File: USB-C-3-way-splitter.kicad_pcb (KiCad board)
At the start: 2 copper layers, 31 x 33 mm, 33 parts, among them J1 USB_C_Receptacle_USB2.0, J2 Conn_01x05_Socket, J3 Conn_01x05_Socket, J4 Conn_01x05_Socket, U1 LM393, U2 SiP32509

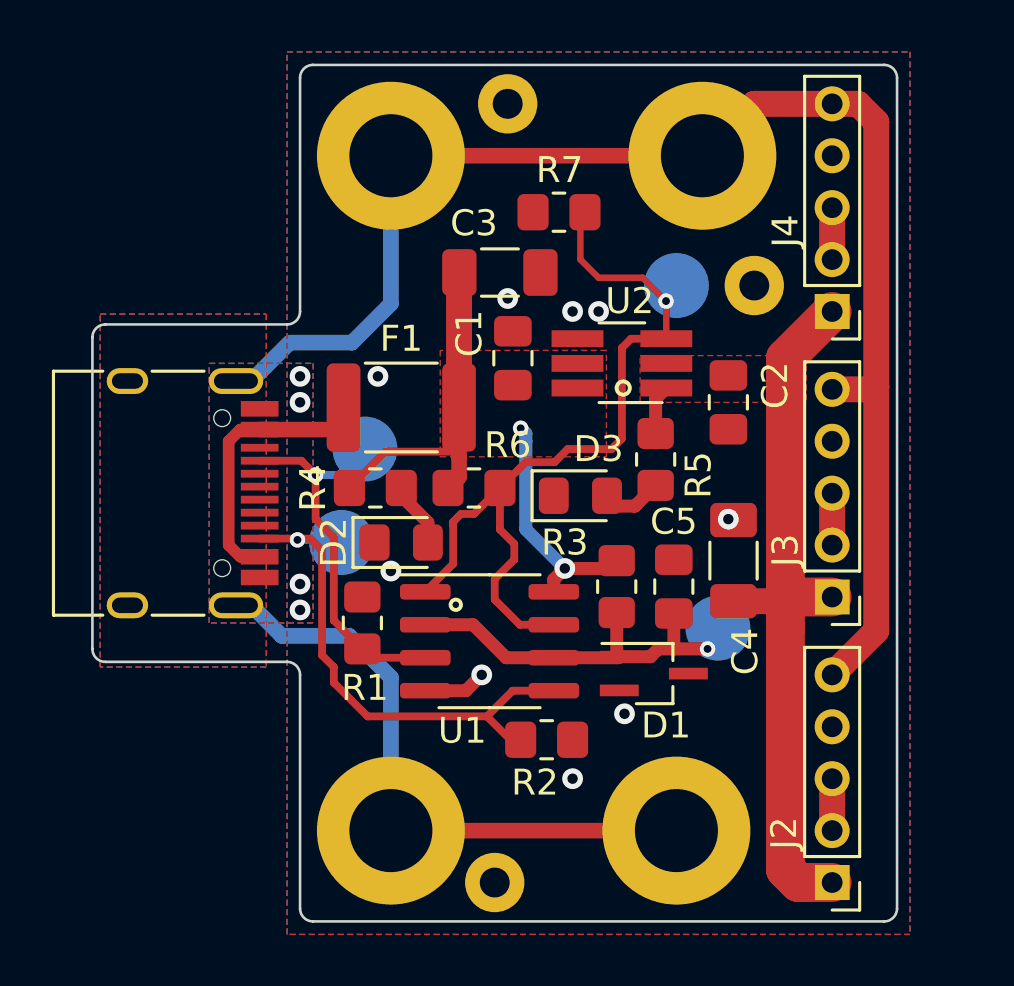
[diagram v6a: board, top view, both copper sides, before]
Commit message: Redesigned to fix circuit design error
The previous revision had the comparator outputs implemented as an AND instead of an OR, which was preventing the switch from ever turning on.
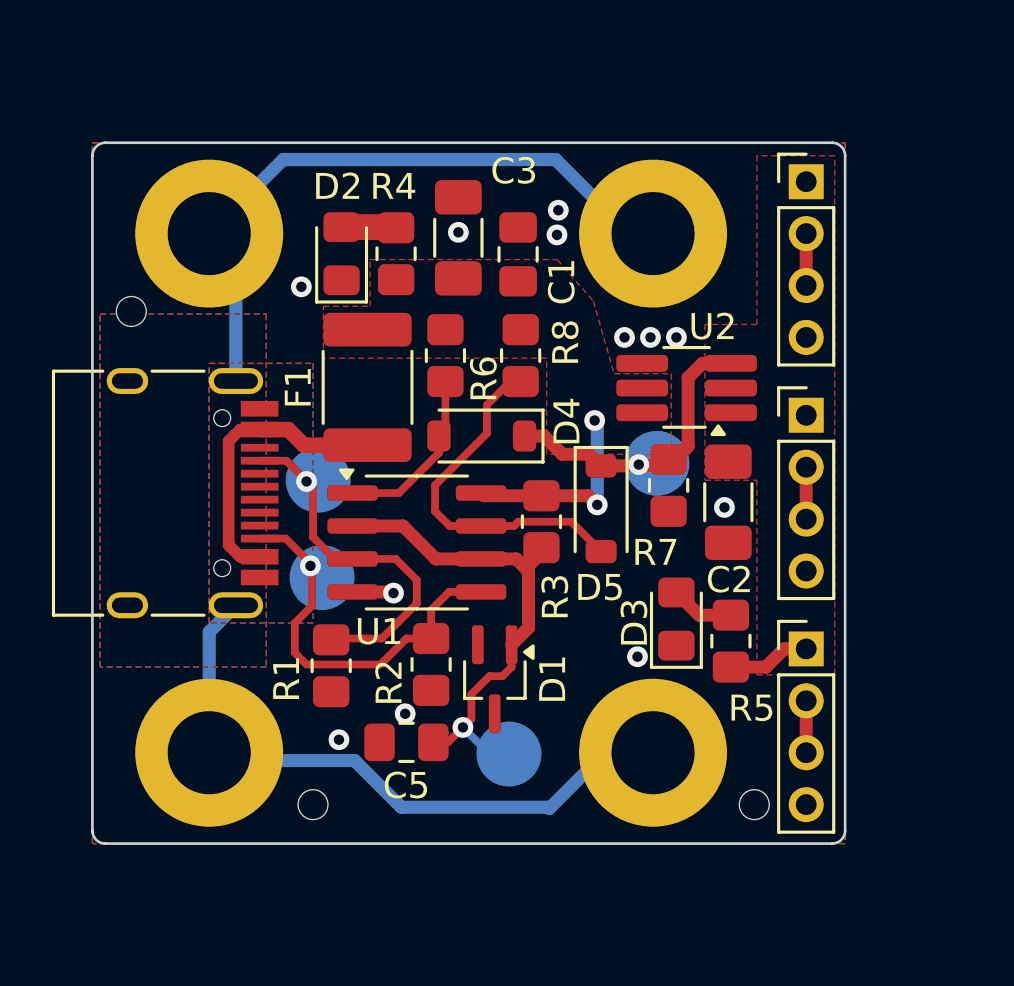
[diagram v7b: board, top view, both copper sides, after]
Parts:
- removed C4: 22uF, Capacitor_SMD:C_1206_3216Metric_Pad1.33x1.80mm_HandSolder
- added D4: 1N4148W, Diode_SMD:D_SOD-123, F.Cu at (13.5, -2.20)
- added D5: 1N4148W, Diode_SMD:D_SOD-123, F.Cu at (18.1, 0.60)
- added R8: 1k, Resistor_SMD:R_0805_2012Metric_Pad1.20x1.40mm_HandSolder, F.Cu at (15.0, -5.30)
- C2: value 100nF -> 22uF; footprint Capacitor_SMD:C_0805_2012Metric_Pad1.18x1.45mm_HandSolder -> Capacitor_SMD:C_1206_3216Metric_Pad1.33x1.80mm_HandSolder
- J2, J3, J4: value Conn_01x05_Socket -> Conn_01x04; footprint Connector_PinHeader_2.00mm:PinHeader_1x05_P2.00mm_Vertical -> Connector_PinHeader_2.00mm:PinHeader_1x04_P2.00mm_Vertical
- moved H2 29.8 mm to (3.00, 10.0)
- moved J2 27.0 mm to (26.0, -12.0), turned to 0 degrees
- moved H3 25.1 mm to (20.1, -10.0)
- moved H7 20.0 mm to (24.0, 12.0)
- moved H5 16.6 mm to (0.00, -7.00)
- moved J4 13.0 mm to (26.0, 6.00), turned to 0 degrees
- moved C5 11.9 mm to (10.6, 9.60), turned to 180 degrees
- moved D2 11.4 mm to (8.10, -9.22), turned to 90 degrees
- moved R7 11.3 mm to (20.7, -0.30), turned to -90 degrees
- moved TP4 9.40 mm to (14.6, 10.1)
- moved R4 9.06 mm to (10.2, -9.22), turned to 90 degrees
- moved H1 7.62 mm to (3.00, -10.0)
- moved H6 7.62 mm to (7.00, 12.0)
- moved R5 7.58 mm to (23.1, 5.70), turned to 90 degrees
- moved J3 7.07 mm to (26.0, -3.00), turned to 0 degrees
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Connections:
- R6 pad 2: EN -> Net-(D4-A)
- U1 pad 1: EN -> Net-(D4-A)
- U1 pad 7: EN -> Net-(D5-A)
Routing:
- net GNDPWR: track 80.5 -> 51.7 mm
- net +5V: track 30.2 -> 3.28 mm
- net EN: track 31.1 -> 11.8 mm
- net VBUS: track 22.7 -> 7.95 mm
- net Net-(D5-A): track 0.00 -> 14.2 mm
- net Net-(D4-A): track 0.00 -> 6.82 mm
- net CC2: track 20.8 -> 15.3 mm
- net +1V2: track 14.6 -> 19.5 mm
- net GND: track 2.43 -> 1.59 mm, vias 13 -> 12
- net CC1: track 14.7 -> 13.9 mm
- net Net-(D2-A): track 2.65 -> 2.11 mm
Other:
- board size 31 x 33 mm -> 29 x 27 mm
- board text added: "+1.2V"
- board text removed: "1.25V"
- board text removed: "5V"
- board text removed: "D+"
- board text removed: "D-"
- board text removed: "GND"
- board text removed: "JLCJLCJLCJLC"
- board text removed: "SHIELD"
- board text removed: "USB-C Splitter V1 Pylon Feb 15 24"

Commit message: Added label
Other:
- board text added: "USB-C Splitter V2 Pylon April 13 24"
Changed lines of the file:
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@@
+		)
+	)
+	(gr_text "USB-C Splitter V2\nPylon April 13 24"
+		(at 17.1 -8.55 90)
+		(layer "B.SilkS")
+		(effects
+			(font
+				(size 1.2 1.2)
+				(thickness 0.2)
+				(bold yes)
+			)
+			(justify left bottom mirror)
 		)
 	)
